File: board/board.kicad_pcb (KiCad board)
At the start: 2 copper layers, 1 part, among them U2 ATxmega128A4U-AU

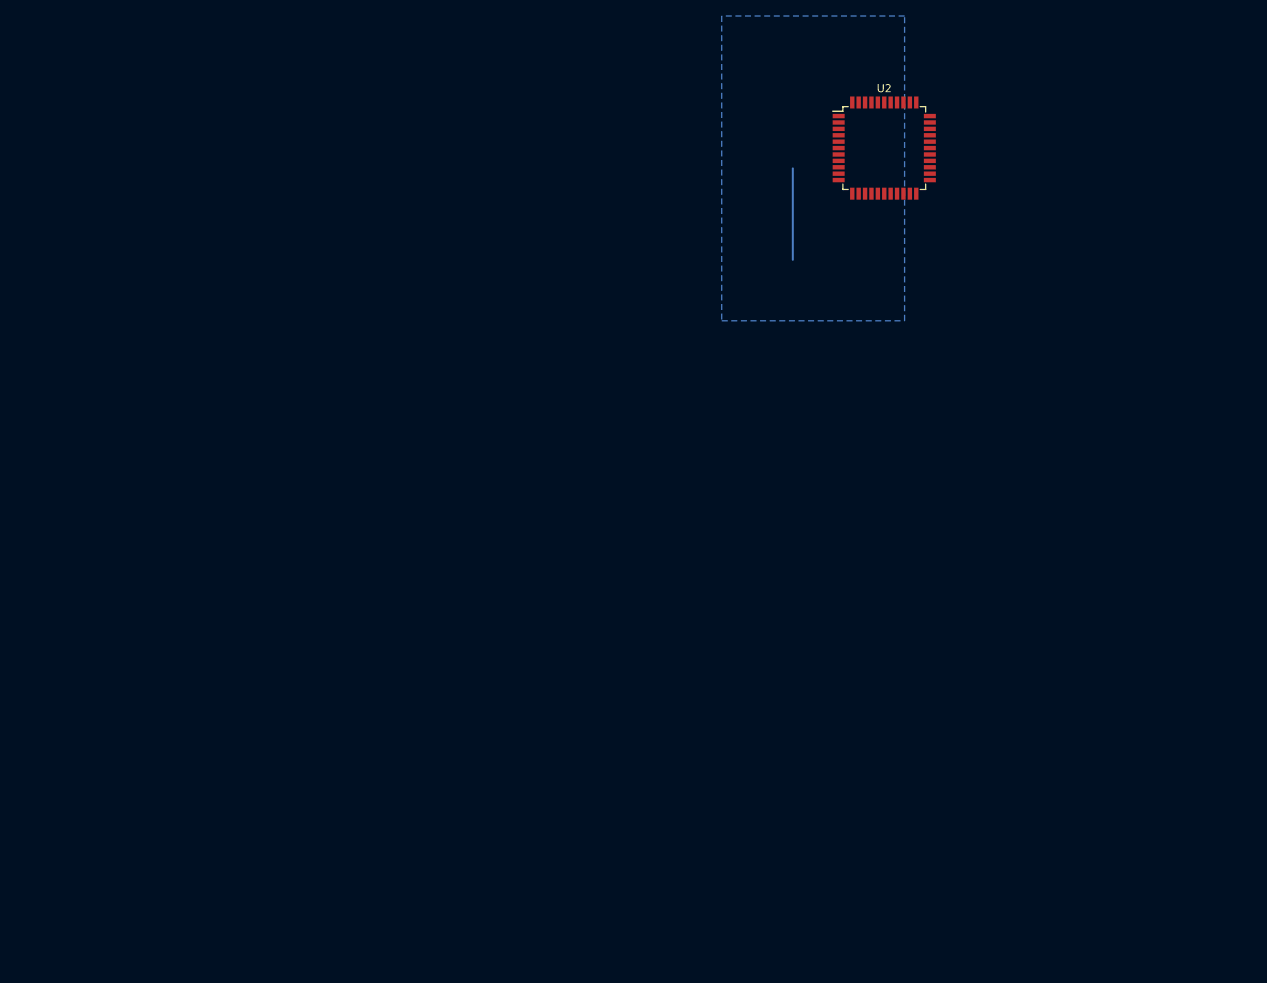
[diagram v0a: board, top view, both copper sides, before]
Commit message: Added solenoid for latch
Because that's important. Whoopsie
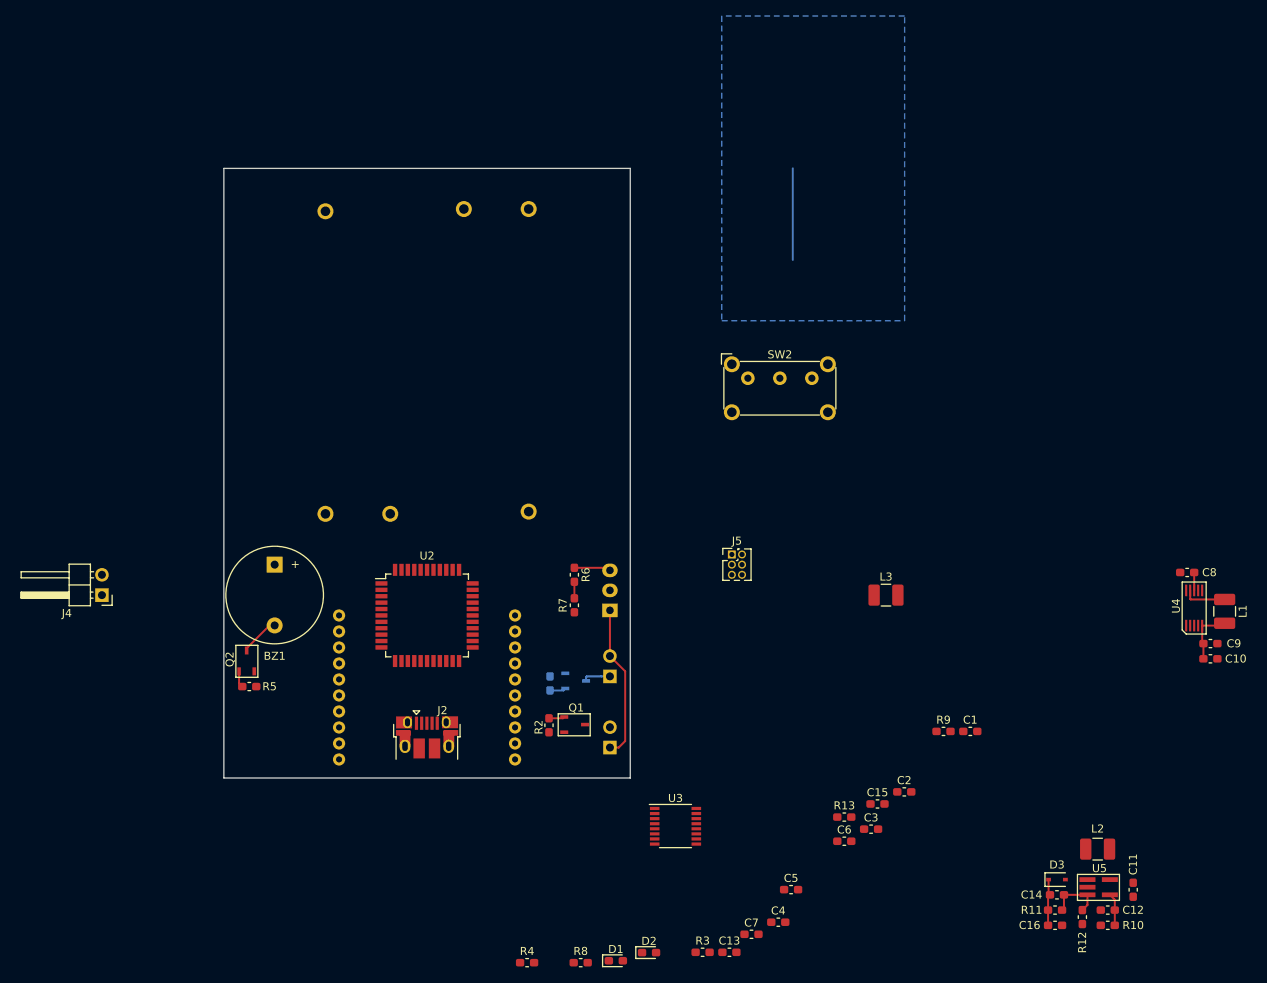
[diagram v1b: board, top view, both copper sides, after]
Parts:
- added BT1: Battery, custom_components:CR123A Battery Holder, B.Cu at (63.5, 94.0)
- added BT2: Battery, custom_components:CR123A Battery Holder, B.Cu at (88.9, 55.9)
- added BZ1: Buzzer, Buzzer_Beeper:Buzzer_12x9.5RM7.6, F.Cu at (57.1, 100.3)
- added C1: 100nF, Capacitor_SMD:C_0603_1608Metric_Pad1.05x0.95mm_HandSolder, F.Cu at (144.1, 121.2)
- added C10: 10uF, Capacitor_SMD:C_0603_1608Metric_Pad1.05x0.95mm_HandSolder, F.Cu at (174.1, 112.1)
- added C11: 1uF, Capacitor_SMD:C_0603_1608Metric_Pad1.05x0.95mm_HandSolder, F.Cu at (164.5, 141.0)
- added C12: C_Small, Capacitor_SMD:C_0603_1608Metric_Pad1.05x0.95mm_HandSolder, F.Cu at (161.3, 143.5)
- added C13: 100nF, Capacitor_SMD:C_0603_1608Metric_Pad1.05x0.95mm_HandSolder, F.Cu at (114.0, 148.8)
- added C14: 15pF, Capacitor_SMD:C_0603_1608Metric_Pad1.05x0.95mm_HandSolder, F.Cu at (154.9, 141.6)
- added C15: 100nF, Capacitor_SMD:C_0603_1608Metric_Pad1.05x0.95mm_HandSolder, F.Cu at (132.5, 130.2)
- added C16: 4.7uF, Capacitor_SMD:C_0603_1608Metric_Pad1.05x0.95mm_HandSolder, F.Cu at (154.7, 145.4)
- added C2: 100nF, Capacitor_SMD:C_0603_1608Metric_Pad1.05x0.95mm_HandSolder, F.Cu at (135.9, 128.7)
- added C3: 100nF, Capacitor_SMD:C_0603_1608Metric_Pad1.05x0.95mm_HandSolder, F.Cu at (131.7, 133.4)
- added C4: 4.7uF, Capacitor_SMD:C_0603_1608Metric_Pad1.05x0.95mm_HandSolder, F.Cu at (120.1, 145.0)
- added C5: 10uF, Capacitor_SMD:C_0603_1608Metric_Pad1.05x0.95mm_HandSolder, F.Cu at (121.7, 141.0)
- added C6: 1uF, Capacitor_SMD:C_0603_1608Metric_Pad1.05x0.95mm_HandSolder, F.Cu at (128.4, 134.9)
- added C7: 47pF, Capacitor_SMD:C_0603_1608Metric_Pad1.05x0.95mm_HandSolder, F.Cu at (116.8, 146.5)
- added C8: 10uF, Capacitor_SMD:C_0603_1608Metric_Pad1.05x0.95mm_HandSolder, F.Cu at (171.2, 101.3)
- added C9: 22uF, Capacitor_SMD:C_0603_1608Metric_Pad1.05x0.95mm_HandSolder, F.Cu at (174.1, 110.2)
- added D1: LED, LED_SMD:LED_0603_1608Metric_Pad1.05x0.95mm_HandSolder, F.Cu at (99.8, 149.8)
- added D2: LED, LED_SMD:LED_0603_1608Metric_Pad1.05x0.95mm_HandSolder, F.Cu at (104.0, 148.8)
- added D3: D, Diode_SMD:D_SOD-323, F.Cu at (154.9, 139.7)
- added J1: Screw_Terminal_01x02, Connector_PinHeader_2.54mm:PinHeader_1x02_P2.54mm_Vertical, B.Cu at (99.1, 114.3)
- added J2: USB_B_Micro, Connector_USB:USB_Micro-B_Amphenol_10103594-0001LF_Horizontal, F.Cu at (76.2, 121.9)
- added J3: Screw_Terminal_01x02, Connector_PinHeader_2.54mm:PinHeader_1x02_P2.54mm_Vertical, B.Cu at (99.1, 123.2)
- added J4: Conn_01x02_Male, Connector_PinHeader_2.54mm:PinHeader_1x02_P2.54mm_Horizontal, F.Cu at (35.6, 104.1)
- added J5: Conn_02x03_Odd_Even, Connector_PinHeader_1.27mm:PinHeader_2x03_P1.27mm_Vertical, F.Cu at (114.3, 99.1)
- added L1: 10uH, Inductor_SMD:L_1210_3225Metric_Pad1.42x2.65mm_HandSolder, F.Cu at (175.9, 106.2)
- added L2: 4.7uH, Inductor_SMD:L_1210_3225Metric_Pad1.42x2.65mm_HandSolder, F.Cu at (160.0, 135.9)
- added L3: 27nH, Inductor_SMD:L_1210_3225Metric_Pad1.42x2.65mm_HandSolder, F.Cu at (133.6, 104.1)
- added Q1: Q_NJFET_GSD, custom_components:NFET Toshiba SSM3K339R, F.Cu at (93.3, 117.5)
- added Q2: Q_NJFET_GSD, custom_components:NFET Toshiba SSM3K339R, F.Cu at (50.8, 113.7)
- added Q3: Q_NJFET_GSD, custom_components:NFET Toshiba SSM3K339R, B.Cu at (93.5, 117.7)
- added R1: 10k, Resistor_SMD:R_0603_1608Metric_Pad1.05x0.95mm_HandSolder, B.Cu at (91.6, 115.2)
- added R10: R_Small, Resistor_SMD:R_0603_1608Metric_Pad1.05x0.95mm_HandSolder, F.Cu at (161.3, 145.4)
- added R11: 432k, Resistor_SMD:R_0603_1608Metric_Pad1.05x0.95mm_HandSolder, F.Cu at (154.7, 143.5)
- added R12: 49.9k, Resistor_SMD:R_0603_1608Metric_Pad1.05x0.95mm_HandSolder, F.Cu at (158.1, 144.4)
- added R13: 10k, Resistor_SMD:R_0603_1608Metric_Pad1.05x0.95mm_HandSolder, F.Cu at (128.4, 131.9)
- added R2: 10k, Resistor_SMD:R_0603_1608Metric_Pad1.05x0.95mm_HandSolder, F.Cu at (91.4, 120.4)
- added R3: 47k, Resistor_SMD:R_0603_1608Metric_Pad1.05x0.95mm_HandSolder, F.Cu at (110.6, 148.8)
- added R4: 10k, Resistor_SMD:R_0603_1608Metric_Pad1.05x0.95mm_HandSolder, F.Cu at (88.7, 150.1)
- added R5: 10k, Resistor_SMD:R_0603_1608Metric_Pad1.05x0.95mm_HandSolder, F.Cu at (54.0, 115.6)
- added R6: 30k, Resistor_SMD:R_0603_1608Metric_Pad1.05x0.95mm_HandSolder, F.Cu at (94.6, 101.6)
- added R7: 10k, Resistor_SMD:R_0603_1608Metric_Pad1.05x0.95mm_HandSolder, F.Cu at (94.6, 105.4)
- added R8: 27, Resistor_SMD:R_0603_1608Metric_Pad1.05x0.95mm_HandSolder, F.Cu at (95.4, 150.1)
- added R9: 27, Resistor_SMD:R_0603_1608Metric_Pad1.05x0.95mm_HandSolder, F.Cu at (140.8, 121.2)
- added SW1: SW_SPDT, Connector_JST:JST_EH_B03B-EH-A_1x03_P2.50mm_Vertical, B.Cu at (99.1, 106.0)
- added SW2: SW_SPDT, Button_Switch_THT:SW_E-Switch_EG1224_SPDT_Angled, F.Cu at (116.3, 77.0)
- added U1: XBee, custom_components:XBee_THT, B.Cu at (76.2, 106.7)
- added U3: FT230XS, Package_SO:SSOP-16_3.9x4.9mm_P0.635mm, F.Cu at (107.3, 133.0)
- added U4: IC_REG_BCK_3.3V, custom_components:10-pin FP TPS62056DGSR, F.Cu at (172.1, 105.8)
- added U5: IC_REG_BOOST_ADJ_1.4A, custom_components:IC REG BOOST SC4503TSKTRT, F.Cu at (158.8, 138.6)
- moved U2 81.7 mm to (76.2, 106.7)
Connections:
- net Net-(U2-Pad19) renamed +3V3
- U2 pad 10: Net-(U2-Pad10) -> /LED1CTRL
- U2 pad 12: Net-(U2-Pad12) -> /USARTC0_TX
- U2 pad 14: Net-(U2-Pad14) -> /LATCH_SENSE
- U2 pad 15: Net-(U2-Pad15) -> /LATCH_ENABLE
- U2 pad 20: Net-(U2-Pad20) -> /LED2CTRL
- U2 pad 22: Net-(U2-Pad22) -> /USARTD0_TX
- U2 pad 23: Net-(U2-Pad23) -> /USARTD0_RX
- U2 pad 24: Net-(U2-Pad24) -> /BUZZER_CTRL
- U2 pad 34: Net-(U2-Pad34) -> /PDI_DATA
- U2 pad 35: Net-(U2-Pad35) -> /PDI_CLK
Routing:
- net Net-(J1-Pad2): track 0.00 -> 19.4 mm
- net +3V3: track 0.00 -> 7.15 mm
- net Net-(C14-Pad2): track 0.00 -> 7.11 mm
- net +12V: track 0.00 -> 5.89 mm
- net Net-(L1-Pad1): track 0.00 -> 5.40 mm
- net Net-(BZ1-Pad2): track 0.00 -> 4.96 mm
- net Net-(R6-Pad1): track 0.00 -> 4.58 mm
- net Net-(C12-Pad1): track 0.00 -> 4.07 mm
- net Net-(J1-Pad1): track 0.00 -> 3.94 mm
- net +6V: track 0.00 -> 2.25 mm
- net /BUZZER_CTRL: track 0.00 -> 2.07 mm
- net /LATCH_SENSE: track 0.00 -> 2.06 mm
- net /E_Match_Fire_1: track 0.00 -> 2.00 mm
- net /E_Match_Fire_2: track 0.00 -> 1.97 mm
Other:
- board outline added: 50.8 x 76.2 mm

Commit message: Fixed footprints, major placements
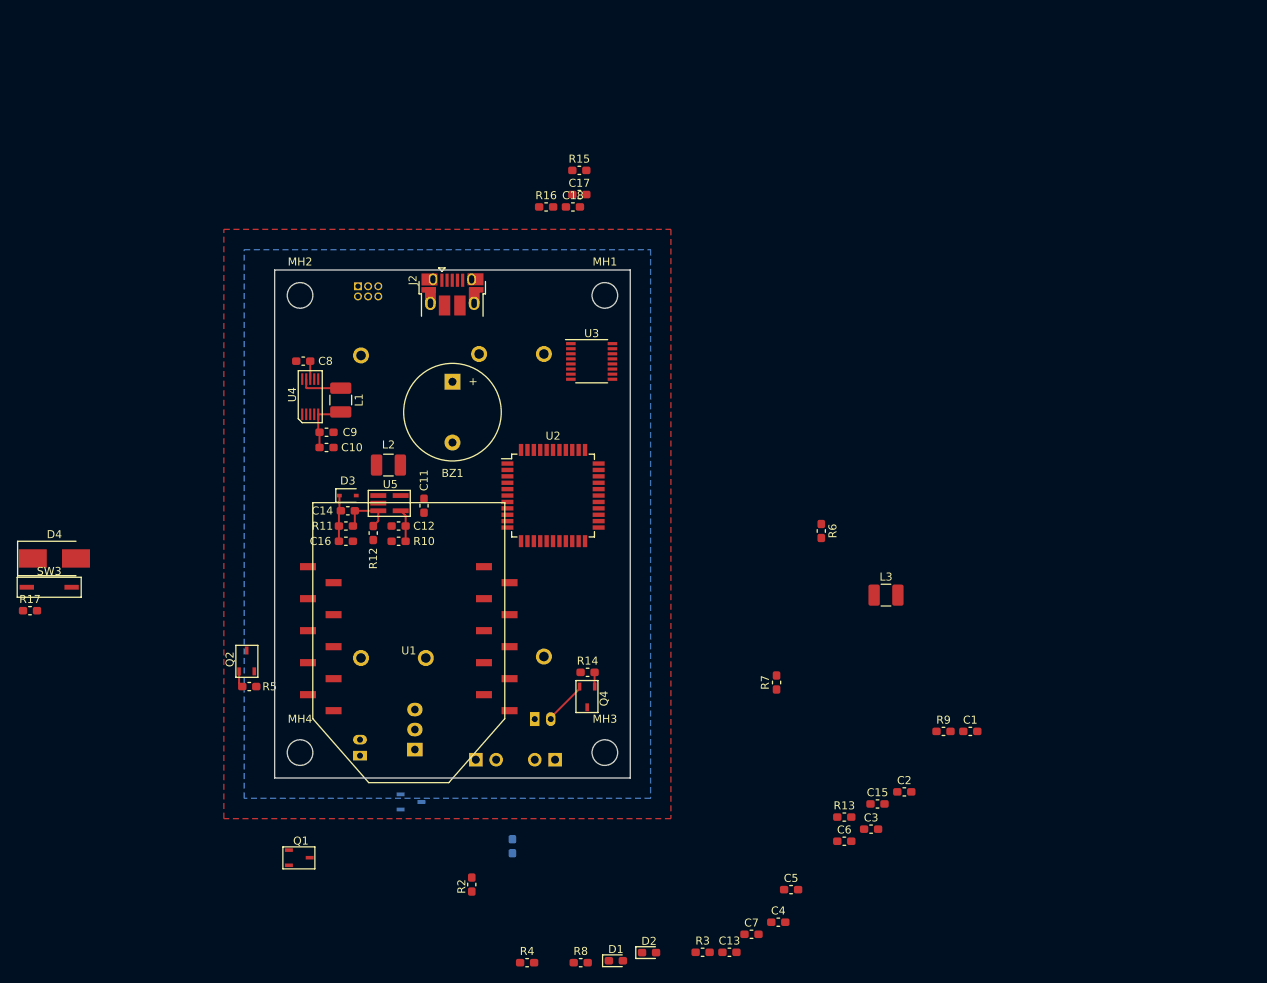
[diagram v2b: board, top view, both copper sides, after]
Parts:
- removed J4: Conn_01x02_Male, Connector_PinHeader_2.54mm:PinHeader_1x02_P2.54mm_Horizontal
- added C17: 47pF, Capacitor_SMD:C_0603_1608Metric_Pad1.05x0.95mm_HandSolder, F.Cu at (95.2, 54.1)
- added C18: 47pF, Capacitor_SMD:C_0603_1608Metric_Pad1.05x0.95mm_HandSolder, F.Cu at (94.4, 55.6)
- added D4: D_Small, Diode_SMD:D_SMB_Handsoldering, F.Cu at (29.6, 99.6)
- added J6: Conn_01x02_Male, Connector_JST:JST_PH_B2B-PH-K_1x02_P2.00mm_Vertical, B.Cu at (89.7, 119.6)
- added MH1: MountingHole, MountingHole:MountingHole_3.2mm_M3, F.Cu at (98.4, 66.7)
- added MH2: MountingHole, MountingHole:MountingHole_3.2mm_M3, F.Cu at (60.3, 66.7)
- added MH3: MountingHole, MountingHole:MountingHole_3.2mm_M3, F.Cu at (98.4, 123.8)
- added MH4: MountingHole, MountingHole:MountingHole_3.2mm_M3, F.Cu at (60.3, 123.8)
- added Q4: Q_NJFET_GSD, custom_components:NFET Toshiba SSM3K339R, F.Cu at (99.1, 115.6)
- added R14: 10k, Resistor_SMD:R_0603_1608Metric_Pad1.05x0.95mm_HandSolder, F.Cu at (96.3, 113.8)
- added R15: 220, Resistor_SMD:R_0603_1608Metric_Pad1.05x0.95mm_HandSolder, F.Cu at (95.2, 51.0)
- added R16: 220, Resistor_SMD:R_0603_1608Metric_Pad1.05x0.95mm_HandSolder, F.Cu at (91.1, 55.6)
- added R17: 10k, Resistor_SMD:R_0603_1608Metric_Pad1.05x0.95mm_HandSolder, F.Cu at (26.6, 106.1)
- added SW3: SW_DIP_x01, custom_components:DIP Switch CHS-01TA, F.Cu at (29.0, 103.2)
- J5: moved to B.Cu
- R6: value 30k -> 10k
- SW2: footprint Button_Switch_THT:SW_E-Switch_EG1224_SPDT_Angled -> Connector_JST:JST_PH_B2B-PH-K_1x02_P2.00mm_Vertical; moved to B.Cu
- U1: footprint custom_components:XBee_THT -> custom_components:XBee_SMD; moved to F.Cu
- moved C10 113.6 mm to (63.6, 85.7)
- moved C9 113.6 mm to (63.6, 83.8)
- moved C8 113.6 mm to (60.7, 74.9)
- moved L1 113.6 mm to (65.4, 79.8)
- moved U4 113.6 mm to (61.6, 79.3)
- moved L2 100.8 mm to (71.4, 87.9)
- moved R12 100.8 mm to (69.5, 96.4)
- moved C11 100.8 mm to (75.8, 93.0)
- moved C14 100.8 mm to (66.3, 93.6)
- moved D3 100.8 mm to (66.3, 91.7)
- moved U5 100.8 mm to (70.1, 90.5)
- moved C12 100.8 mm to (72.6, 95.5)
- moved C16 100.8 mm to (66.1, 97.4)
- moved R10 100.8 mm to (72.6, 97.4)
- moved R11 100.8 mm to (66.1, 95.5)
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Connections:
- D1 pad 1: GND -> Net-(D1-Pad1)
- D2 pad 1: GND -> Net-(D2-Pad1)
- U2 pad 12: /USARTC0_TX -> /USARTC0_RX
- U2 pad 13: /USARTC0_RX -> /USARTC0_TX
- U2 pad 22: /USARTD0_TX -> /USARTD0_RX
- U2 pad 23: /USARTD0_RX -> /USARTD0_TX
- U2 pad 40: Net-(U2-Pad40) -> /SOLENOID_CTRL
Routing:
- net Net-(J1-Pad2): track 19.4 -> 0.00 mm
- net /USARTC0_RX: track 11.4 -> 0.00 mm
- net Net-(D4-Pad2): track 0.00 -> 5.55 mm
- net Net-(BZ1-Pad2): track 4.96 -> 0.27 mm
- net Net-(R6-Pad1): track 4.58 -> 0.00 mm
- net Net-(J1-Pad1): track 3.94 -> 0.00 mm
- net /LATCH_SENSE: track 2.06 -> 0.00 mm
- net /E_Match_Fire_1: track 2.00 -> 0.00 mm
- net /E_Match_Fire_2: track 1.97 -> 0.00 mm
- net /SOLENOID_CTRL: track 0.00 -> 1.79 mm
- added copper zone on F.Cu, net GND
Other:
- board size 50.8 x 76.2 mm -> 44.4 x 63.5 mm

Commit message: Finished placement, began routing
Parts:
- D1, D2, R13, R15, R16, R3, SW3: moved to B.Cu
- Q3, R1: moved to F.Cu
- moved R13 86.1 mm to (69.0, 69.6), turned to 180 degrees
- moved R3 81.7 mm to (86.0, 70.9)
- moved R8 79.8 mm to (86.1, 70.9), turned to 180 degrees
- moved R4 78.8 mm to (100.1, 72.1), turned to 270 degrees
- moved C2 77.9 mm to (86.1, 68.8)
- moved R9 77.8 mm to (86.1, 65.8), turned to 180 degrees
- moved C4 75.4 mm to (93.7, 74.4)
- moved R15 73.7 mm to (78.0, 122.7), turned to 270 degrees
- moved SW3 71.6 mm to (90.2, 66.0)
- moved C1 69.8 mm to (93.7, 72.9)
- moved C3 68.9 mm to (93.7, 75.9)
- moved D4 65.0 mm to (94.5, 103.1)
- moved R17 63.9 mm to (89.9, 114.6)
- moved R16 63.0 mm to (82.8, 118.1), turned to 180 degrees
- moved C15 62.0 mm to (91.2, 84.1)
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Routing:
- net +12V: track 5.89 -> 34.9 mm
- net +3V3: track 7.15 -> 33.6 mm, vias 0 -> 1
- net +6V: track 2.25 -> 25.2 mm
- net /VBUS_SENSE: track 0.00 -> 17.3 mm, vias 0 -> 1
- net /USB_D+: track 0.00 -> 15.0 mm, vias 0 -> 2
- net Net-(D4-Pad2): track 5.55 -> 19.4 mm
- net /FTDI_DECOUPLED_V: track 0.00 -> 11.1 mm
- net /USB_D-: track 0.00 -> 8.25 mm
- net Net-(BZ1-Pad2): track 0.27 -> 8.34 mm
- net Net-(D3-Pad2): track 0.00 -> 6.66 mm
- net Net-(C1-Pad1): track 0.00 -> 6.60 mm
- net Net-(J2-Pad1): track 0.00 -> 5.87 mm, vias 0 -> 1
- net /PDI_CLK: track 0.00 -> 4.85 mm
- net Net-(R6-Pad1): track 0.00 -> 4.49 mm
- net Net-(C15-Pad2): track 0.00 -> 3.83 mm
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
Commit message: Routed :)
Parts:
- added C19: 100nF, Capacitor_SMD:C_0603_1608Metric_Pad1.05x0.95mm_HandSolder, F.Cu at (92.7, 99.3)
- added C20: 100nF, Capacitor_SMD:C_0603_1608Metric_Pad1.05x0.95mm_HandSolder, F.Cu at (84.1, 93.2)
- J1, J3: footprint Connector_PinHeader_2.54mm:PinHeader_1x02_P2.54mm_Vertical -> custom_components:2 pin 2.54mm screw terminal OSTVN02A150
- moved Q2 14.2 mm to (84.3, 88.9)
- moved R5 14.0 mm to (84.1, 89.8)
- moved Q4 8.03 mm to (92.5, 120.1), turned to 180 degrees
- moved J6 7.18 mm to (96.8, 118.6)
- moved R16 4.93 mm to (80.0, 122.2), turned to 90 degrees
- moved C8 3.35 mm to (58.9, 77.7), turned to 90 degrees
- moved J1 1.55 mm to (83.8, 124.5), turned to 0 degrees
- moved R4 1.52 mm to (98.6, 72.1)
- moved J3 1.30 mm to (90.9, 124.5), turned to 180 degrees
- moved C18 1.27 mm to (80.5, 72.1), turned to 270 degrees
- moved R6 1.27 mm to (73.4, 115.0)
- moved R7 1.27 mm to (71.6, 115.0)
- moved R14 0.51 mm to (96.8, 113.8), turned to 180 degrees
- moved R15 0.51 mm to (78.0, 122.2), turned to 90 degrees
- moved C10 0.34 mm to (63.6, 85.3)
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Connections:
- C1 pad 1: Net-(C1-Pad1) -> +3V3
- C3 pad 1: Net-(C1-Pad1) -> +3V3
- C4 pad 1: Net-(C1-Pad1) -> +3V3
- U3 pad 12: Net-(C1-Pad1) -> +3V3
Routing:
- net +3V3: track 33.6 -> 194.0 mm, vias 1 -> 2
- net +6V: track 25.2 -> 98.3 mm, vias 0 -> 1
- net Net-(R17-Pad1): track 2.54 -> 56.6 mm, vias 0 -> 1
- net /PDI_DATA: track 0.00 -> 45.8 mm
- net /PDI_CLK: track 4.85 -> 44.9 mm, vias 0 -> 2
- net /E_Match_Fire_2: track 0.00 -> 39.1 mm, vias 0 -> 2
- net /USARTC0_TX: track 0.00 -> 36.0 mm, vias 0 -> 1
- net /USARTD0_TX: track 0.00 -> 35.9 mm, vias 0 -> 2
- net /SOLENOID_CTRL: track 1.79 -> 36.7 mm, vias 0 -> 2
- net /LED2CTRL: track 0.00 -> 34.7 mm, vias 0 -> 3
- net /USARTD0_RX: track 0.00 -> 33.8 mm, vias 0 -> 2
- net /E_Match_Fire_1: track 0.00 -> 31.2 mm, vias 0 -> 2
- net /LATCH_SENSE: track 1.78 -> 32.6 mm, vias 0 -> 2
- net /LED1CTRL: track 0.00 -> 29.7 mm, vias 0 -> 1
- net Net-(BT1-Pad2): track 0.00 -> 23.9 mm
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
